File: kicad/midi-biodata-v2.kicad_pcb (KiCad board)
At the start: 2 copper layers, 63.5 x 45.7 mm, 46 parts, among them J1 DIN-5_180degree, J2 Audio-Jack-2, J3 Conn_01x02, J4 Conn_01x02, SW1 SW_Push, U1 ATMEGA328P-AU, U2 POT_SWITCH, U3 LMC555xM, Y1 Crystal_GND2

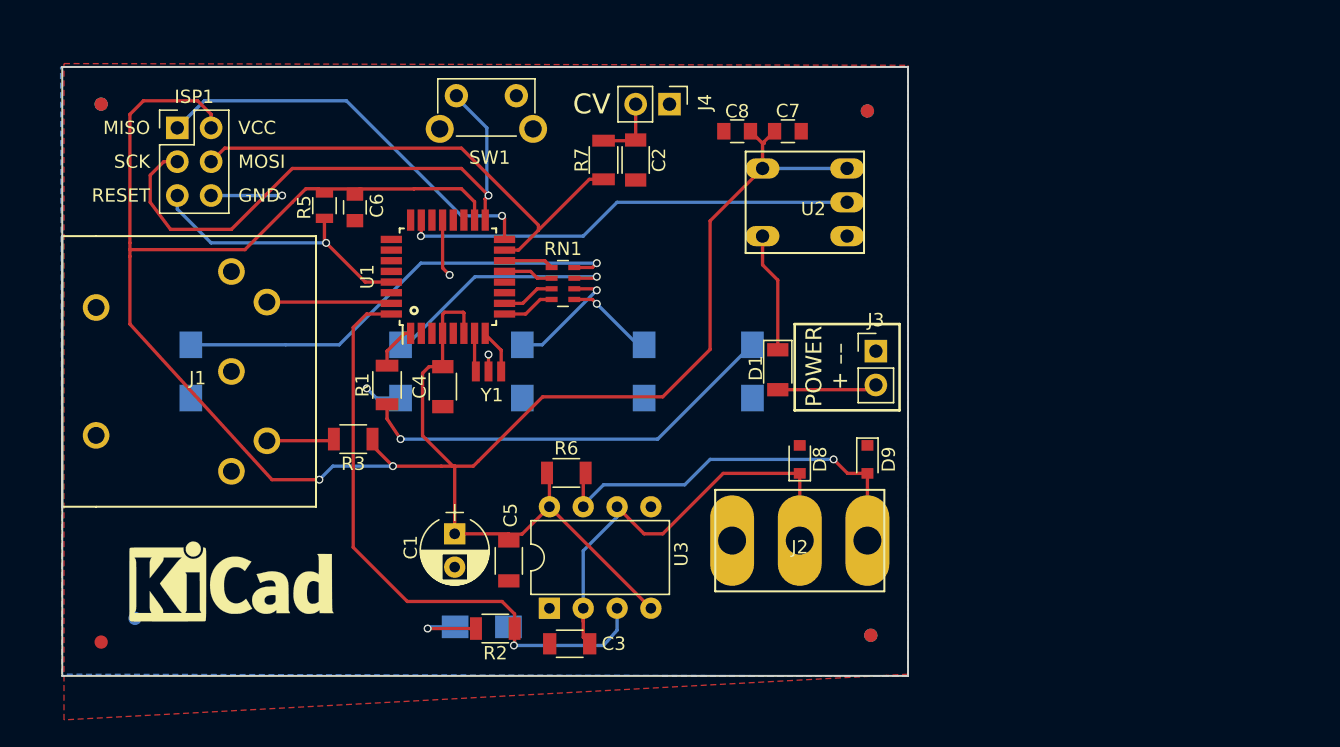
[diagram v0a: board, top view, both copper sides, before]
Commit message: Removed MCU from board, added proper midi out
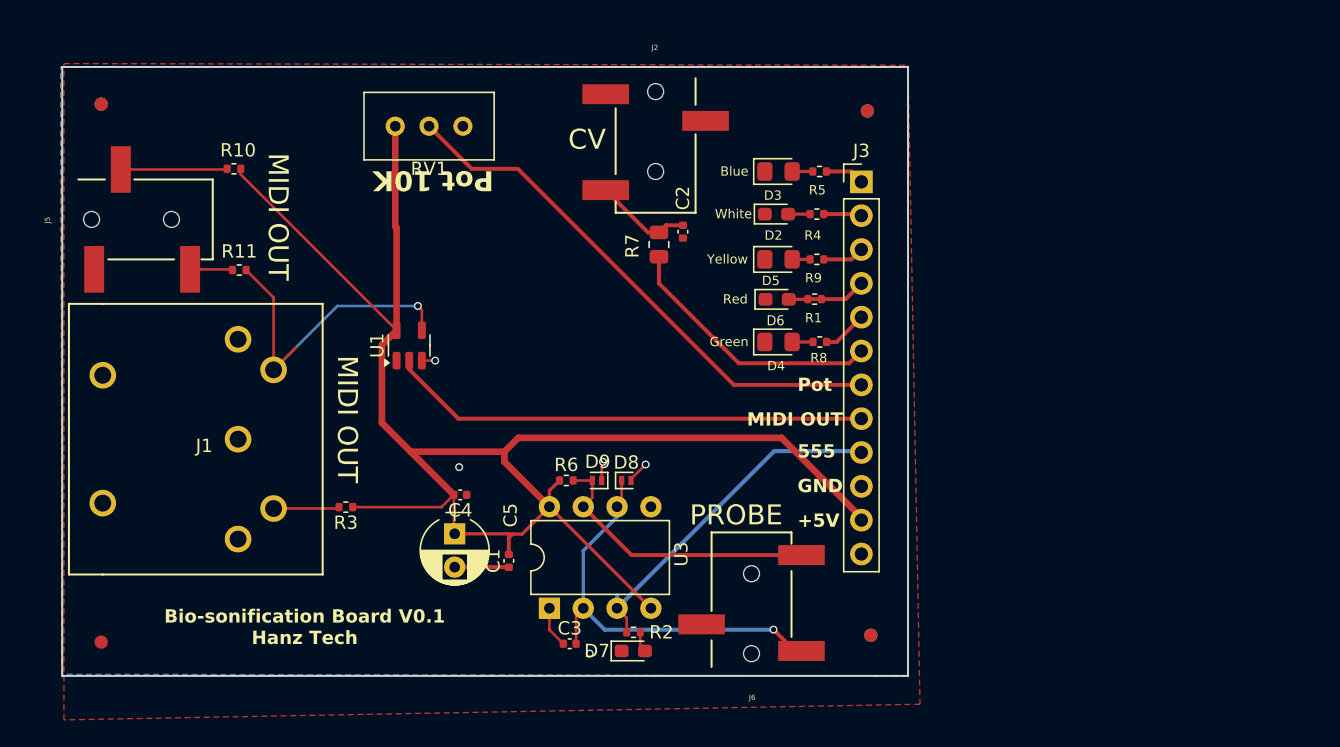
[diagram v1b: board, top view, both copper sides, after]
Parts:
- removed the ? at (5.46, -4.45)
- removed C6, C7: 100nF, Capacitors_SMD:C_0805
- removed C8: 1uF, Capacitors_SMD:C_0805
- removed D1: D, Diodes_SMD:D_1206
- removed G***: LOGO, OPENHARDWARE:OSHWLOGO0.3IN
- removed ISP1: AVR-ISP-6, Pin_Headers:Pin_Header_Straight_2x03_Pitch2.54mm
- removed J4: Conn_01x02, Pin_Headers:Pin_Header_Straight_1x02_Pitch2.54mm
- removed REF**: WEEE-Logo_4.2x6mm_SilkScreen, Symbol:WEEE-Logo_4.2x6mm_SilkScreen
- removed REF**: CE-Logo_8.5x6mm_SilkScreen, Symbol:CE-Logo_8.5x6mm_SilkScreen
- removed REF**: KiCad-Logo_6mm_SilkScreen, Symbol:KiCad-Logo_6mm_SilkScreen
- removed RN1: R_Pack04, Resistors_SMD:R_Array_Concave_4x0603
- removed SW1: SW_Push, Buttons_Switches_ThroughHole:SW_Tactile_SPST_Angled
- removed U2: POT_SWITCH, pot_switch:POT_SWITCH
- removed Y1: Crystal_GND2, pot_switch:murata-cstce
- added J5: PJ-320B, poma:3.5mm_stereo_jack_PJ320B, F.Cu at (2.20, -34.4)
- added J6: PJ-320B, poma:3.5mm_stereo_jack_PJ320B, F.Cu at (51.8, -1.80)
- added R10: 220R, Resistor_SMD:R_0402_1005Metric, F.Cu at (12.9, -38.2)
- added R11: 220R, Resistor_SMD:R_0402_1005Metric, F.Cu at (13.3, -30.6)
- added R4: 220R, Resistor_SMD:R_0402_1005Metric, F.Cu at (56.7, -34.8)
- added R8: 220R, Resistor_SMD:R_0402_1005Metric, F.Cu at (56.9, -25.2)
- added R9: 220R, Resistor_SMD:R_0402_1005Metric, F.Cu at (56.7, -31.4)
- added RV1: Pot 10K, Potentiometer_THT:Potentiometer_Bourns_3296W_Vertical, F.Cu at (25.0, -41.4)
- C1, C2, C4: value 100nF -> 0.1uF; footprint Capacitors_SMD:C_1206 -> Capacitor_SMD:C_0402_1005Metric
- C3: value 4,7nF -> 4.7nF; footprint Capacitors_SMD:C_1206 -> Capacitor_SMD:C_0402_1005Metric
- C5: value 1µF -> 1uF
- D2, D6, D7: footprint LEDs:LED_1206_HandSoldering -> Diode_SMD:D_0603_1608Metric_Pad1.05x0.95mm_HandSolder; moved to F.Cu
- D3, D4, D5: footprint LEDs:LED_1206_HandSoldering -> Diode_SMD:D_0805_2012Metric_Pad1.15x1.40mm_HandSolder; moved to F.Cu
- D8, D9: footprint Diodes_SMD:D_0805 -> Diode_SMD:D_SOD-882
- J2: value Audio-Jack-2 -> PJ-320B; footprint mono-jack:mono-jack -> poma:3.5mm_stereo_jack_PJ320B
- J3: value Conn_01x02 -> Conn_01x14_Pin; footprint Pin_Headers:Pin_Header_Straight_1x02_Pitch2.54mm -> Connector_PinHeader_2.54mm:PinHeader_1x12_P2.54mm_Vertical
- R1, R2, R3, R6: footprint Resistors_SMD:R_1206 -> Resistor_SMD:R_0402_1005Metric
- R5: value 10K -> 220R; footprint Resistors_SMD:R_0805 -> Resistor_SMD:R_0402_1005Metric
- R7: value 3,9K -> 3.9K; footprint Resistors_SMD:R_1206 -> Resistor_SMD:R_0805_2012Metric
- U1: value ATMEGA328P-AU -> SN74LVC1G07DBVR; footprint Housings_QFP:TQFP-32_7x7mm_Pitch0.8mm -> Package_TO_SOT_SMD:SOT-23-5
- moved D2 45.5 mm to (53.6, -34.8), turned to 0 degrees
- moved R5 37.3 mm to (56.9, -38.0), turned to 0 degrees
- moved J2 35.4 mm to (44.5, -44.0)
- moved R1 32.7 mm to (56.5, -28.4), turned to 0 degrees
- moved D3 32.1 mm to (53.8, -38.0), turned to 0 degrees
- moved D9 20.4 mm to (40.1, -14.8), turned to 180 degrees
- moved D4 19.4 mm to (53.8, -25.2), turned to 0 degrees
- moved D5 13.1 mm to (53.8, -31.4), turned to 0 degrees
- moved D8 13.1 mm to (42.4, -14.8), turned to 0 degrees
- moved J3 12.8 mm to (60.0, -37.2)
- moved D7 11.5 mm to (42.9, -2.00), turned to 0 degrees
- moved R2 10.4 mm to (42.9, -3.40), turned to 0 degrees
- moved C4 8.23 mm to (29.9, -13.7), turned to 180 degrees
- moved R7 7.59 mm to (44.8, -32.5)
- moved C2 6.45 mm to (46.6, -33.5)
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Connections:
- C1 pad 2: VCC -> +5V
- C3 pad 2: Net-(C3-Pad2) -> Net-(D8-A1)
- C4 pad 2: VCC -> +5V
- C5 pad 1: VCC -> +5V
- D3 pad 2: Net-(D3-Pad2) -> Net-(D3-A)
- D8 pad 1: Net-(C3-Pad2) -> Net-(D8-A1)
- D9 pad 2: Net-(D9-Pad2) -> Net-(D9-A2)
- J1 pad 1: Net-(J1-Pad1) -> unconnected-(J1-Pad1)
- J1 pad 3: Net-(J1-Pad3) -> unconnected-(J1-Pad3)
- J1 pad 5: Net-(J1-Pad5) -> /MIDI_1_BUF_OUT
- J2 pad 1: Net-(D9-Pad2) -> GND
- J2 pad 2: Net-(C3-Pad2) -> Net-(C2-Pad1)
- J2 pad 3: (no net) -> unconnected-(J2-Pad3)
- J3 pad 1: GND -> LED_BLUE
- J3 pad 2: Net-(D1-Pad2) -> LED_WHITE
- R1 pad 2: Net-(R1-Pad2) -> LED_RED
- R3 pad 1: VCC -> +5V
- R5 pad 1: VCC -> Net-(D3-A)
- R5 pad 2: RESET -> LED_BLUE
- R6 pad 1: VCC -> +5V
- R6 pad 2: Net-(D9-Pad2) -> Net-(D9-A2)
- R7 pad 2: MOSI -> CV
- U1 pad 1: Net-(R1-Pad2) -> unconnected-(U1-NC-Pad1)
- U1 pad 2: Net-(U1-Pad2) -> MIDI_OUT
- U1 pad 4: VCC -> /MIDI_1_BUF_OUT
- U1 pad 5: GND -> +5V
- U3 pad 2: Net-(C3-Pad2) -> Net-(D8-A1)
- U3 pad 4: VCC -> +5V
- U3 pad 5: Net-(U3-Pad5) -> unconnected-(U3-CV-Pad5)
- U3 pad 6: Net-(C3-Pad2) -> Net-(D8-A1)
- U3 pad 7: Net-(D9-Pad2) -> Net-(D9-A2)
- U3 pad 8: VCC -> +5V
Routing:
- net VCC: track 179.3 -> 0.00 mm, vias 2 -> 0
- net +5V: track 9.33 -> 123.5 mm
- net SCK: track 44.8 -> 0.00 mm, vias 1 -> 0
- net POT_1: track 0.00 -> 40.5 mm
- net MOSI: track 37.4 -> 0.00 mm
- net MIDI_OUT: track 0.00 -> 36.5 mm
- net Net-(U1-Pad23): track 34.3 -> 0.00 mm, vias 1 -> 0
- net Net-(C3-Pad2): track 33.6 -> 0.00 mm
- net Net-(D9-Pad2): track 33.6 -> 0.00 mm, vias 1 -> 0
- net Net-(D2-A): track 35.2 -> 1.65 mm, vias 1 -> 0
- net Net-(D8-A1): track 0.00 -> 32.9 mm, vias 0 -> 1
- net Net-(D6-A): track 32.3 -> 1.43 mm, vias 1 -> 0
- net MISO: track 30.7 -> 0.00 mm, vias 1 -> 0
- net /MIDI_1_BUF_OUT: track 0.00 -> 25.6 mm, vias 0 -> 1
- net RESET: track 22.1 -> 0.00 mm, vias 1 -> 0
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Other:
- net class Default removed
- board text added: "+5V"
- board text added: "555"
- board text added: "Bio-sonification Board V0.1 Hanz Tech"
- board text added: "Blue"
- board text added: "Green"
- board text added: "MIDI OUT"
- board text added: "PROBE"
- board text added: "Pot"
- board text added: "Pot 10K"
- board text added: "Red"
- board text added: "White"
- board text added: "Yellow"
- board text removed: "13-37.org electronics MIDI Biodata Sonification Device (2.1.1)"
- board text removed: "B"
- board text removed: "G"
- board text removed: "MISO"
- board text removed: "MOSI"
- board text removed: "POWER + ––"
- board text removed: "RESET"
- board text removed: "SCK"
- board text removed: "VCC"
- board text removed: "W"

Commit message: send to jlcpcb
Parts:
- removed the ? at (2.92, -43.1)
- removed the ? at (60.5, -42.5)
- removed the ? at (60.7, -3.17)
- J3: footprint Connector_PinHeader_2.54mm:PinHeader_1x12_P2.54mm_Vertical -> Connector_PinHeader_2.54mm:PinHeader_1x13_P2.54mm_Vertical
- RV1: footprint Potentiometer_THT:Potentiometer_Bourns_3296W_Vertical -> Potentiometer_THT:Potentiometer_Alps_RK09K_Single_Vertical
- moved RV1 10.4 mm to (25.2, -31.0), turned to 90 degrees
- moved R9 2.08 mm to (57.2, -33.4)
- moved R1 2.04 mm to (56.9, -30.4)
- moved R5 2.04 mm to (57.2, -40.0)
- moved R4 2.01 mm to (56.9, -36.8)
- moved R8 2.00 mm to (57.0, -27.2)
- moved D2 2.00 mm to (53.6, -36.8)
- moved D3 2.00 mm to (53.8, -40.0)
- moved D4 2.00 mm to (53.8, -27.2)
- moved D5 2.00 mm to (53.8, -33.4)
- moved D6 2.00 mm to (53.7, -30.4)
- moved J3 0.53 mm to (60.0, -37.8)
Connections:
- ? pad ~: (no net) -> GND (x4)
- J3 pad 12: +3V3 -> +5V
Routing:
- net +5V: track 123.5 -> 115.6 mm
- net POT_1: track 40.5 -> 36.1 mm
- net LED_RED: track 4.44 -> 2.93 mm
- net GND: track 11.5 -> 10.1 mm, vias 5 -> 40
- net LED_GREEN: track 3.74 -> 2.56 mm
- net CV: track 20.1 -> 19.3 mm
- net LED_BLUE: track 2.95 -> 3.71 mm
- net LED_WHITE: track 2.88 -> 3.47 mm
- net Net-(D5-A): track 1.35 -> 1.93 mm
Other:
- board text added: "MIDI Out"

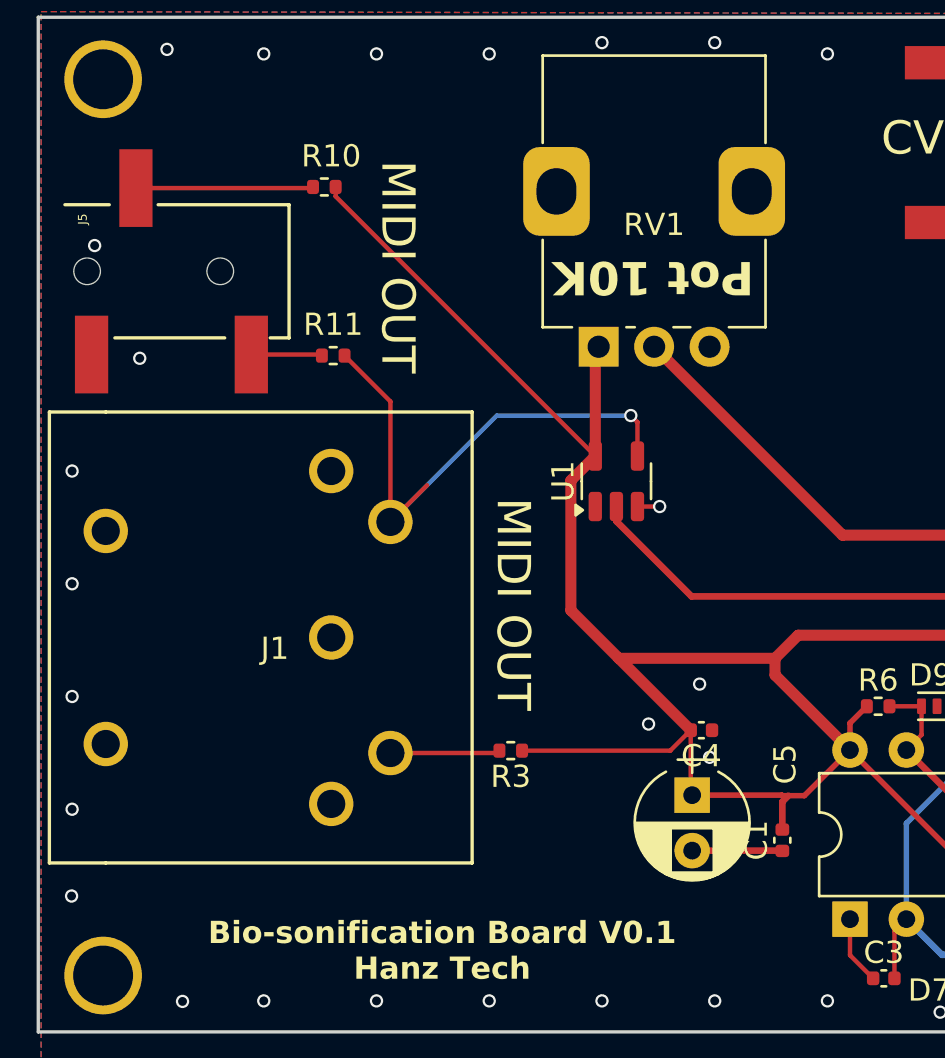
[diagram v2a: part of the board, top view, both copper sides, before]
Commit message: fixed midi routing on the pcb board
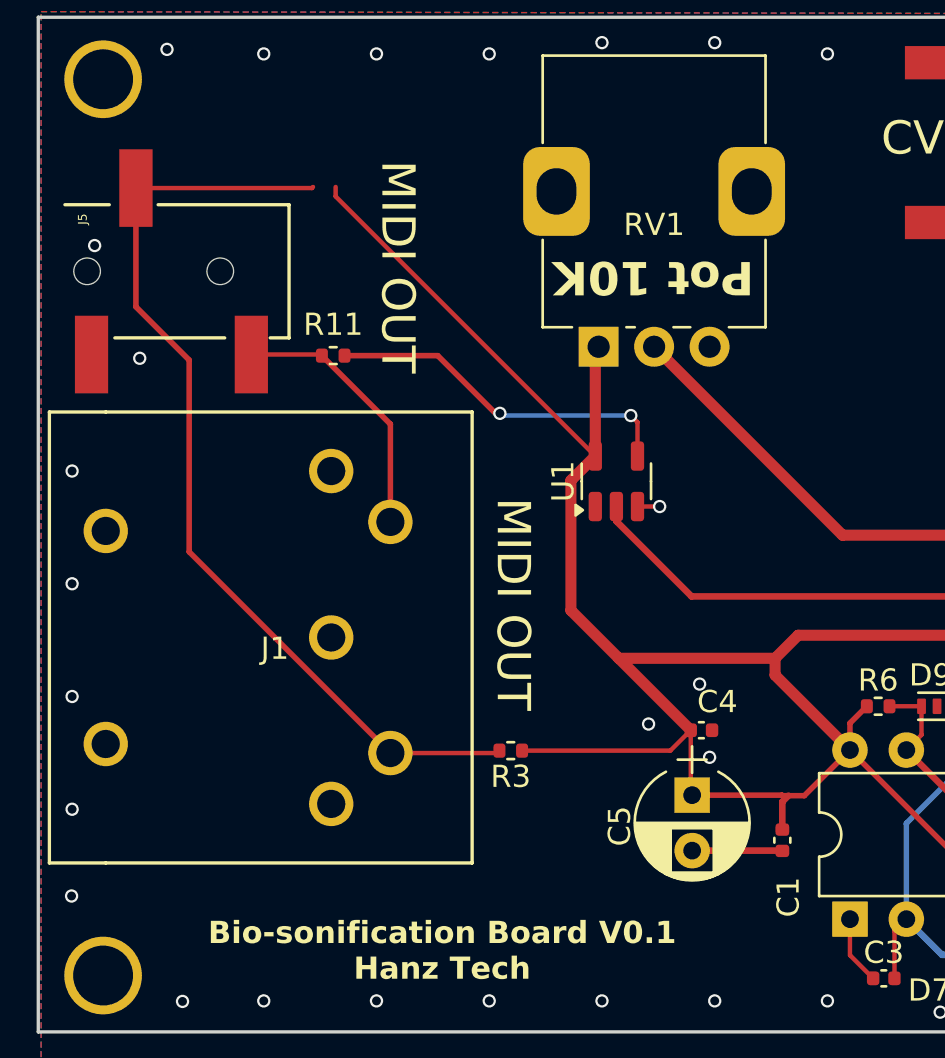
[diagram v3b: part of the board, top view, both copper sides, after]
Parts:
- removed R10: 220R, Resistor_SMD:R_0402_1005Metric
- C5: value 1uF -> 100uF
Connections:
- J1 pad 5: /MIDI_1_BUF_OUT -> Net-(J1-Pad5)
- J5 pad 2: Net-(J5-Pad2) -> Net-(J1-Pad5)
- J5 pad 3: Net-(J5-Pad3) -> Net-(J1-Pad4)
- R11 pad 1: Net-(J5-Pad2) -> Net-(J1-Pad5)
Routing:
- net Net-(J1-Pad4): track 4.96 -> 43.4 mm
- net Net-(J1-Pad5): track 0.00 -> 12.2 mm
- net /MIDI_1_BUF_OUT: track 25.6 -> 16.2 mm, vias 1 -> 2
- net Net-(J5-Pad3): track 8.25 -> 0.00 mm
- net Net-(J5-Pad2): track 3.45 -> 0.00 mm

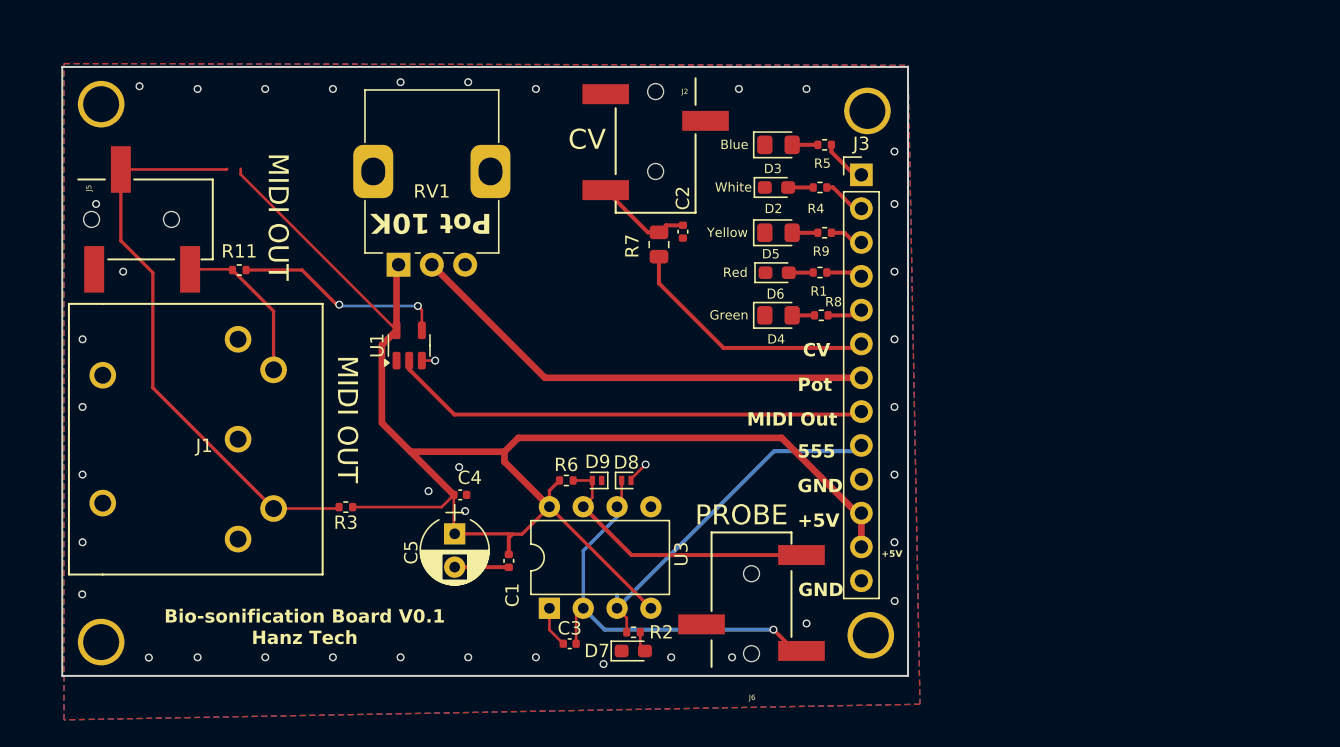
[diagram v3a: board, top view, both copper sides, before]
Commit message: cleanup, changed footprint for 3.5mm jack
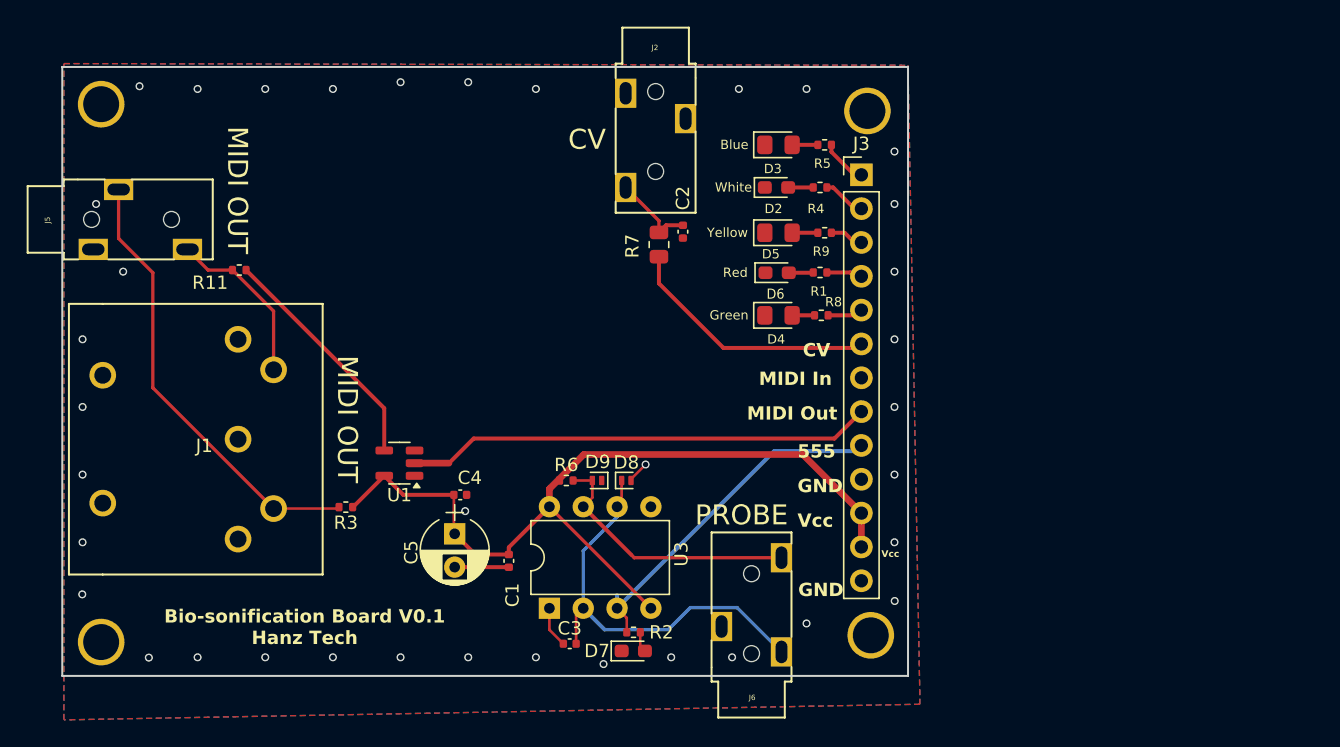
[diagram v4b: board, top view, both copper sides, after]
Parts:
- removed RV1: Pot 10K, Potentiometer_THT:Potentiometer_Alps_RK09K_Single_Vertical
- J2, J5, J6: footprint poma:3.5mm_stereo_jack_PJ320B -> poma:3.5mm_stereo_jack_PJ320B_THRU
- moved U1 8.87 mm to (25.3, -16.1), turned to 180 degrees
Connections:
- net +5V renamed VCC
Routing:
- net VCC: track 115.6 -> 68.0 mm
- net POT_1: track 36.1 -> 0.38 mm
- net Net-(J1-Pad4): track 43.4 -> 33.7 mm
- net /MIDI_1_BUF_OUT: track 16.2 -> 17.8 mm, vias 2 -> 0
- net Net-(D8-A1): track 32.9 -> 31.3 mm, vias 1 -> 0
- net Net-(D9-A2): track 21.6 -> 20.2 mm
- net GND: track 10.1 -> 9.11 mm, vias 40 -> 37
- net MIDI_OUT: track 36.5 -> 35.6 mm
- net Net-(C2-Pad1): track 7.38 -> 6.47 mm
- net Net-(J1-Pad5): track 12.2 -> 12.9 mm
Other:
- board text added: "MIDI In"
- board text added: "Vcc"
- board text removed: "+5V"
- board text removed: "Pot"
- board text removed: "Pot 10K"
- board text removed: "Y"
